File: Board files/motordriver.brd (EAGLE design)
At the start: 30.1 x 44.5 mm, 13 parts, among them Q1 IPB034N03L, U1 VNH5019A

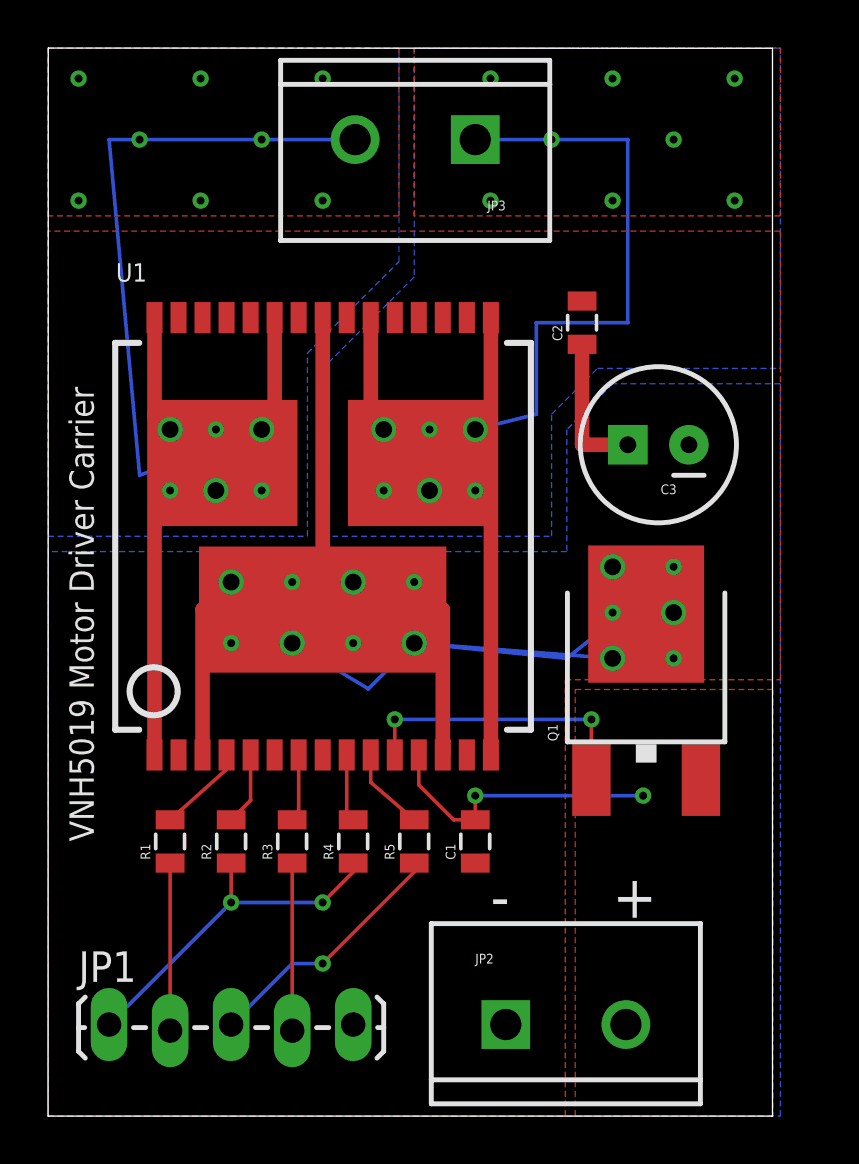
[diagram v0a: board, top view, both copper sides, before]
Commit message: Fixed slightly misaligned board outline
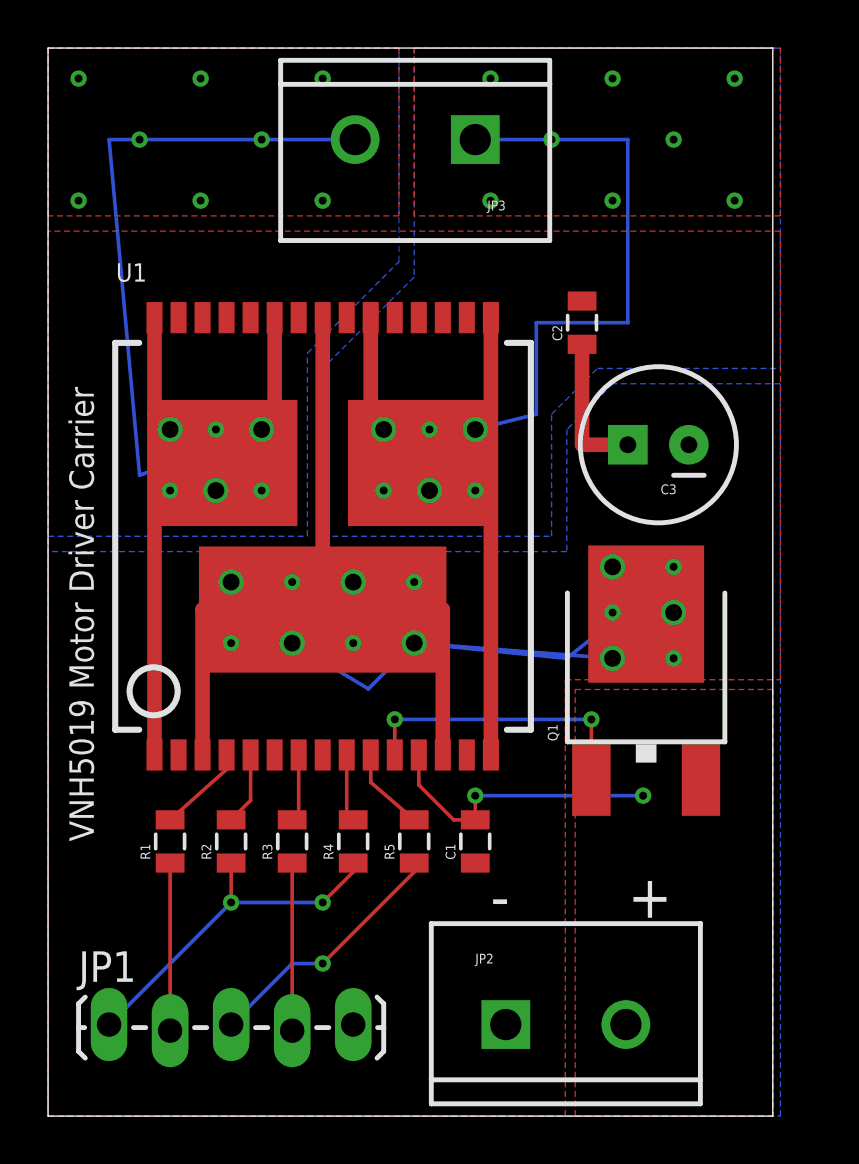
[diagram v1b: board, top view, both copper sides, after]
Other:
- board size 30.1 x 44.5 mm -> 30.2 x 44.5 mm
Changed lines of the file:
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@@
 <board>
 <plain>
-<wire x1="0" y1="0" x2="30.15" y2="0" width="0" layer="20"/>
-<wire x1="30.15" y1="0" x2="30.15" y2="44.44" width="0" layer="20"/>
-<wire x1="30.15" y1="44.44" x2="0.01" y2="44.45" width="0" layer="20"/>
-<wire x1="0.01" y1="44.45" x2="0" y2="0" width="0" layer="20"/>
+<wire x1="0" y1="0" x2="30.1625" y2="0" width="0" layer="20"/>
+<wire x1="30.1625" y1="0" x2="30.1625" y2="44.45" width="0" layer="20"/>
+<wire x1="30.1625" y1="44.45" x2="0" y2="44.45" width="0" layer="20"/>
+<wire x1="0" y1="44.45" x2="0" y2="0" width="0" layer="20"/>
 <text x="1.905" y="11.43" size="1.016" layer="21" rot="R90">VNH5019 Motor Driver Carrier</text>
-<text x="23.495" y="8.255" size="1.778" layer="21">+</text>
+<text x="24.13" y="8.255" size="1.778" layer="21">+</text>
 <text x="18.415" y="8.255" size="1.778" layer="21">-</text>
 </plain>

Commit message: Added labels and removed some thermals
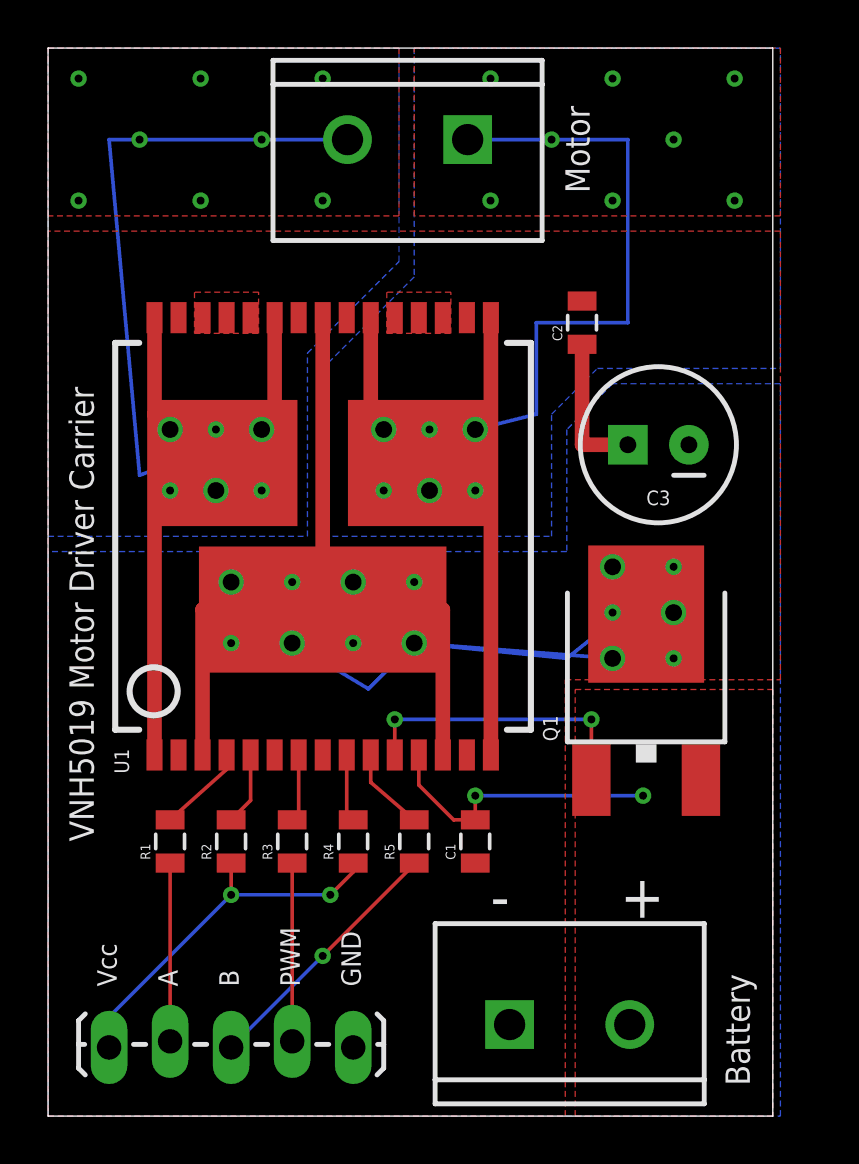
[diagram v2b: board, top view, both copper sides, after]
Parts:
- moved JP1 10.2 mm to (12.7, 2.86), turned to 180 degrees
- moved JP3 0.32 mm to (17.5, 40.6)
- moved JP2 0.16 mm to (19.2, 3.81)
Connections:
- net 3.3V: now also JP1.5; no longer JP1.1
- net GND: now also JP1.1; no longer JP1.5
- net N$7: now also JP1.4; no longer JP1.2
- net N$8: now also JP1.2; no longer JP1.4
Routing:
- net 3.3V: track 14.8 -> 15.6 mm
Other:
- board text added: "A"
- board text added: "B"
- board text added: "Battery"
- board text added: "GND"
- board text added: "Motor"
- board text added: "PWM"
- board text added: "Vcc"
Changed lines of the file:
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@@
 <setting verticaltext="up"/>
 </settings>
-<grid distance="0.05" unitdist="inch" unit="inch" style="dots" multiple="1" display="no" altdistance="0.025" altunitdist="inch" altunit="inch"/>
+<grid distance="0.05" unitdist="inch" unit="inch" style="dots" multiple="1" display="no" altdistance="0.0125" altunitdist="inch" altunit="inch"/>
 <layers>
 <layer number="1" name="Top" color="4" fill="1" visible="yes" active="yes"/>
@@
 <wire x1="0" y1="44.45" x2="0" y2="0" width="0" layer="20"/>
 <text x="1.905" y="11.43" size="1.016" layer="21" rot="R90">VNH5019 Motor Driver Carrier</text>
-<text x="24.13" y="8.255" size="1.778" layer="21">+</text>
+<text x="23.8125" y="8.255" size="1.778" layer="21">+</text>
 <text x="18.415" y="8.255" size="1.778" layer="21">-</text>
+<text x="2.8575" y="5.3975" size="0.8128" layer="21" rot="R90">Vcc</text>
+<text x="5.3975" y="5.3975" size="0.8128" layer="21" rot="R90">A</text>
+<text x="7.9375" y="5.3975" size="0.8128" layer="21" rot="R90">B</text>
+<text x="10.4775" y="5.3975" size="0.8128" layer="21" rot="R90">PWM</text>
+<text x="13.0175" y="5.3975" size="0.8128" layer="21" rot="R90">GND</text>
+<text x="29.21" y="1.27" size="1.016" layer="21" rot="R90">Battery</text>
+<text x="22.5425" y="38.4175" size="1.016" layer="21" rot="R90">Motor</text>
 </plain>
 <attributes>
@@
 </autorouter>
 <elements>
-<element name="U1" library="Custom" package="MULTIPOWERSO-30" value="VNH5019A" x="11.43" y="24.13"/>
-<element name="JP2" library="SparkFun-Connectors" package="SCREWTERMINAL-5MM-2" value="BATTERY" x="19.05" y="3.81"/>
-<element name="JP1" library="SparkFun-Connectors" package="1X05_LOCK_LONGPADS" value="" x="2.54" y="3.81"/>
-<element name="JP3" library="SparkFun-Connectors" package="SCREWTERMINAL-5MM-2" value="MOTOR" x="17.78" y="40.64" rot="R180"/>
-<element name="Q1" library="SparkFun-DiscreteSemi" package="DPAK" value="IPB034N03L" x="24.892" y="19.304">
+<element name="U1" library="Custom" package="MULTIPOWERSO-30" value="VNH5019A" x="11.43" y="24.13" smashed="yes">
+<attribute name="NAME" x="3.37" y="14.255" size="0.6096" layer="25" rot="R90"/>
+</element>
+<element name="JP2" library="SparkFun-Connectors" package="SCREWTERMINAL-5MM-2" value="BATTERY" x="19.20875" y="3.81" smashed="yes"/>
+<element name="JP1" library="SparkFun-Connectors" package="1X05_LOCK_LONGPADS" value="" x="12.7" y="2.8575" smashed="yes" rot="R180">
+<attribute name="VALUE" x="13.97" y="6.1595" size="1.27" layer="27" font="vector" rot="R180"/>
+</element>
+<element name="JP3" library="SparkFun-Connectors" package="SCREWTERMINAL-5MM-2" value="MOTOR" x="17.4625" y="40.64" smashed="yes" rot="R180"/>
+<element name="Q1" library="SparkFun-DiscreteSemi" package="DPAK" value="IPB034N03L" x="24.892" y="19.304" smashed="yes">
 <attribute name="PROD_ID" value="TRANS-09984" x="24.892" y="19.304" size="1.778" layer="27" display="off"/>
+<attribute name="NAME" x="21.209" y="15.602" size="0.6096" layer="25" rot="R90"/>
 </element>
 <element name="C1" library="SparkFun-Capacitors" package="0805" value="0.1uF" x="17.78" y="11.43" rot="R90"/>
 <element name="C2" library="SparkFun-Capacitors" package="0805" value="0.1uF" x="22.225" y="33.02" rot="R90"/>
-<element name="C3" library="SparkFun-Capacitors" package="CPOL-RADIAL-100UF-25V" value="47uF" x="25.4" y="27.94" rot="R180"/>
+<element name="C3" library="SparkFun-Capacitors" package="CPOL-RADIAL-100UF-25V" value="47uF" x="25.4" y="27.94" smashed="yes" rot="R180">
+<attribute name="NAME" x="25.4" y="26.035" size="0.6096" layer="25" rot="R180" align="bottom-center"/>
+</element>
 <element name="R1" library="SparkFun-Resistors" package="0805" value="1k" x="5.08" y="11.43" rot="R90"/>
 <element name="R5" library="SparkFun-Resistors" package="0805" value="1k" x="15.24" y="11.43" rot="R90"/>
@@
 <signal name="GND">
 <contactref element="JP2" pad="1"/>
-<contactref element="JP1" pad="5"/>
+<contactref element="JP1" pad="1"/>
 <contactref element="U1" pad="26"/>
 <contactref element="U1" pad="27"/>
@@
 <vertex x="0" y="36.83"/>
 </polygon>
+<polygon width="0" layer="1" thermals="no">
+<vertex x="6.096" y="32.5755"/>
+<vertex x="8.763" y="32.5755"/>
+<vertex x="8.763" y="34.29"/>
+<vertex x="6.096" y="34.29"/>
+</polygon>
+<polygon width="0" layer="1" thermals="no">
+<vertex x="14.097" y="32.5755"/>
+<vertex x="16.764" y="32.5755"/>
+<vertex x="16.764" y="34.29"/>
+<vertex x="14.097" y="34.29"/>
+</polygon>
 </signal>
 <signal name="VIN">
@@
 <wire x1="24.13" y1="33.02" x2="24.13" y2="40.64" width="0.1524" layer="16"/>
 <wire x1="24.13" y1="40.64" x2="20.955" y2="40.64" width="0.1524" layer="16"/>
-<wire x1="20.955" y1="40.64" x2="17.78" y2="40.64" width="0.1524" layer="16"/>
+<wire x1="20.955" y1="40.64" x2="17.4625" y2="40.64" width="0.1524" layer="16"/>
 <wire x1="18.43" y1="33.23" x2="18.43" y2="15.03" width="0.6096" layer="1"/>
 <wire x1="18.43" y1="33.23" x2="18.43" y2="29.21" width="0.1524" layer="1"/>
@@
 <wire x1="2.54" y1="40.64" x2="3.81" y2="40.64" width="0.1524" layer="16"/>
 <wire x1="3.81" y1="40.64" x2="8.89" y2="40.64" width="0.1524" layer="16"/>
-<wire x1="8.89" y1="40.64" x2="12.78" y2="40.64" width="0.1524" layer="16"/>
+<wire x1="8.89" y1="40.64" x2="12.4625" y2="40.64" width="0.1524" layer="16"/>
 <wire x1="4.43" y1="33.23" x2="4.43" y2="29.21" width="0.6096" layer="1"/>
 <wire x1="4.43" y1="29.21" x2="4.43" y2="15.03" width="0.6096" layer="1"/>
@@
 </signal>
 <signal name="3.3V">
-<contactref element="JP1" pad="1"/>
+<contactref element="JP1" pad="5"/>
 <contactref element="R2" pad="1"/>
 <contactref element="R4" pad="1"/>
-<wire x1="7.62" y1="10.53" x2="7.62" y2="8.89" width="0.1524" layer="1"/>
-<via x="7.62" y="8.89" extent="1-16" drill="0.3302"/>
-<wire x1="7.62" y1="8.89" x2="2.54" y2="3.81" width="0.1524" layer="16"/>
+<wire x1="2.54" y1="2.8575" x2="2.54" y2="4.1275" width="0.1524" layer="16"/>
+<wire x1="2.54" y1="4.1275" x2="7.62" y2="9.2075" width="0.1524" layer="16"/>
+<via x="7.62" y="9.2075" extent="1-16" drill="0.3302"/>
+<wire x1="7.62" y1="9.2075" x2="7.62" y2="10.53" width="0.1524" layer="1"/>
 <wire x1="12.7" y1="10.53" x2="12.7" y2="10.16" width="0.1524" layer="1"/>
-<wire x1="12.7" y1="10.16" x2="11.43" y2="8.89" width="0.1524" layer="1"/>
-<via x="11.43" y="8.89" extent="1-16" drill="0.3302"/>
-<wire x1="11.43" y1="8.89" x2="7.62" y2="8.89" width="0.1524" layer="16"/>
+<wire x1="12.7" y1="10.16" x2="11.7475" y2="9.2075" width="0.1524" layer="1"/>
+<via x="11.7475" y="9.2075" extent="1-16" drill="0.3302"/>
+<wire x1="11.7475" y1="9.2075" x2="7.62" y2="9.2075" width="0.1524" layer="16"/>
 </signal>
 <signal name="N$1">
@@
 <contactref element="R5" pad="1"/>
 <contactref element="JP1" pad="3"/>
-<wire x1="7.62" y1="3.81" x2="10.16" y2="6.35" width="0.1524" layer="16"/>
-<wire x1="10.16" y1="6.35" x2="11.43" y2="6.35" width="0.1524" layer="16"/>
-<via x="11.43" y="6.35" extent="1-16" drill="0.3302"/>
-<wire x1="11.43" y1="6.35" x2="15.24" y2="10.16" width="0.1524" layer="1"/>
-<wire x1="15.24" y1="10.16" x2="15.24" y2="10.53" width="0.1524" layer="1"/>
+<wire x1="7.62" y1="2.8575" x2="11.43" y2="6.6675" width="0.1524" layer="16"/>
+<via x="11.43" y="6.6675" extent="1-16" drill="0.3302"/>
+<wire x1="11.43" y1="6.6675" x2="15.24" y2="10.4775" width="0.1524" layer="1"/>
+<wire x1="15.24" y1="10.4775" x2="15.24" y2="10.53" width="0.1524" layer="1"/>
 </signal>
 <signal name="N$7">
+<contactref element="JP1" pad="4"/>
+<contactref element="R1" pad="1"/>
+<wire x1="5.08" y1="10.53" x2="5.08" y2="3.1115" width="0.1524" layer="1"/>
+</signal>
+<signal name="N$8">
 <contactref element="JP1" pad="2"/>
-<contactref element="R1" pad="1"/>
-<wire x1="5.08" y1="10.53" x2="5.08" y2="3.556" width="0.1524" layer="1"/>
-</signal>
-<signal name="N$8">
-<contactref element="JP1" pad="4"/>
 <contactref element="R3" pad="1"/>
-<wire x1="10.16" y1="10.53" x2="10.16" y2="3.556" width="0.1524" layer="1"/>
+<wire x1="10.16" y1="10.53" x2="10.16" y2="3.1115" width="0.1524" layer="1"/>
 </signal>
 <signal name="N$9">
